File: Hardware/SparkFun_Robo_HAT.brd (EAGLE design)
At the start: 65.1 x 57 mm, 244 parts, among them J11 EXT MTR PWR, J18 ISP, J2 RASPBERRYPI-40-PIN-GPIO_SMD_S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, J20 USB C, J23 CORTEX_JTAG_DEBUG_PTH, J7 EXT SERVO PWR, J8 EXT 5V PWR, Q1 310mA/60V/1.6Ω, Q23 20V/0.2A/8MHz/1.2Ω/1Vth, Q24 20V/0.2A/8MHz/1.2Ω/1Vth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

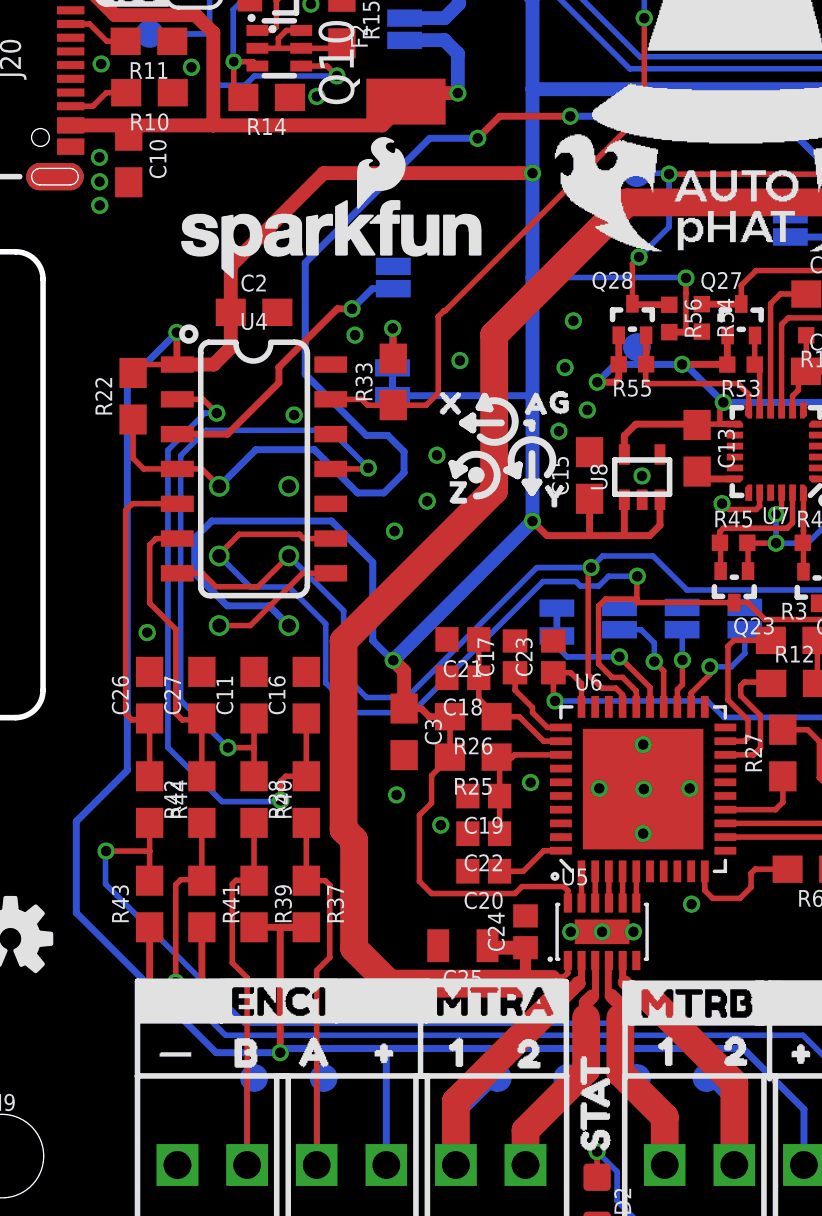
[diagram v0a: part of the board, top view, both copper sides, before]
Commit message: added test point to 3.3V rail
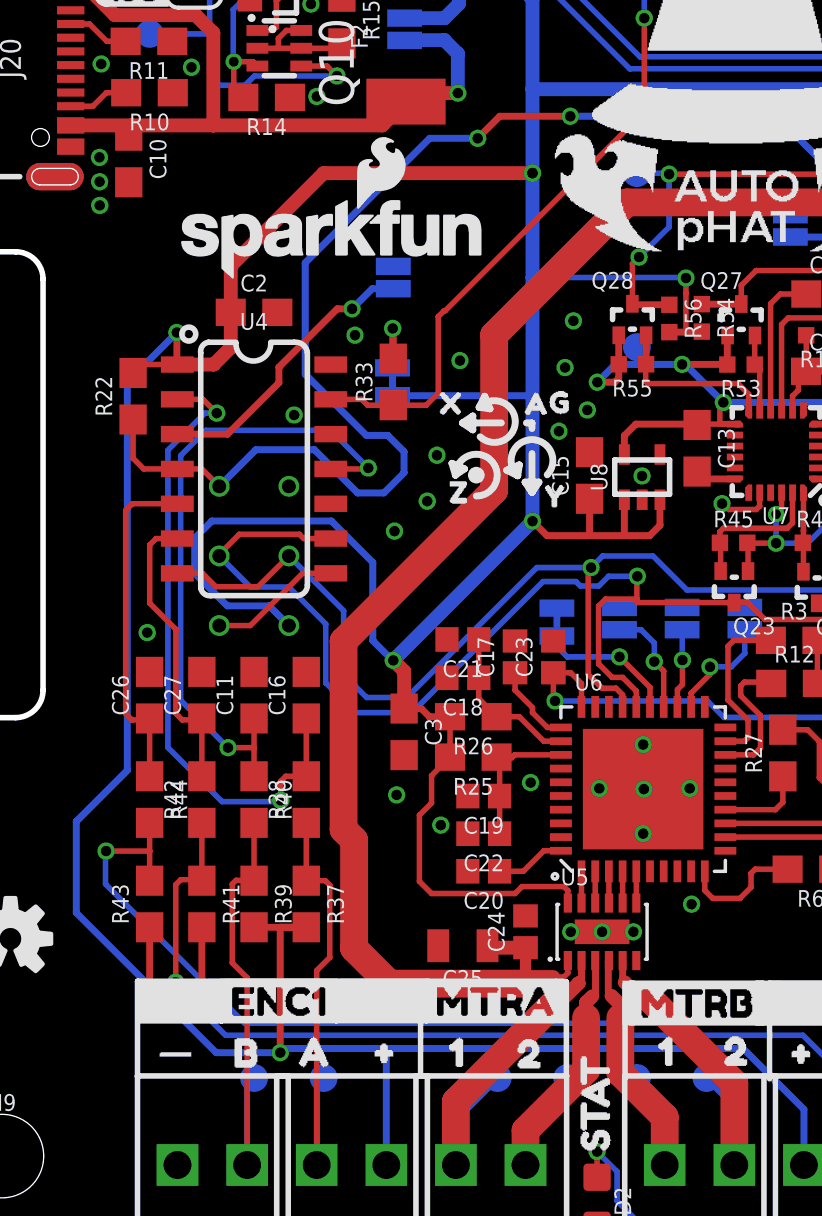
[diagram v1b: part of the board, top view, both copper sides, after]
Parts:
- added TP19: (no value), SparkFun-Connectors:TP_15TH
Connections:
- net 3.3V: now also TP19.P$1
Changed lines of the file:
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@@
 <grid distance="0.05" unitdist="inch" unit="inch" style="lines" multiple="1" display="yes" altdistance="0.001" altunitdist="inch" altunit="inch"/>
 <layers>
-<layer number="1" name="Top" color="4" fill="1" visible="yes" active="yes"/>
+<layer number="1" name="Top" color="4" fill="1" visible="no" active="yes"/>
 <layer number="15" name="Route15" color="4" fill="6" visible="no" active="no"/>
 <layer number="16" name="Bottom" color="1" fill="1" visible="yes" active="yes"/>
@@
 <layer number="18" name="Vias" color="2" fill="1" visible="yes" active="yes"/>
 <layer number="19" name="Unrouted" color="6" fill="1" visible="yes" active="yes"/>
-<layer number="20" name="Dimension" color="24" fill="1" visible="yes" active="yes"/>
-<layer number="21" name="tPlace" color="16" fill="1" visible="yes" active="yes"/>
+<layer number="20" name="Dimension" color="24" fill="1" visible="no" active="yes"/>
+<layer number="21" name="tPlace" color="16" fill="1" visible="no" active="yes"/>
 <layer number="22" name="bPlace" color="14" fill="1" visible="yes" active="yes"/>
-<layer number="23" name="tOrigins" color="15" fill="1" visible="yes" active="yes"/>
+<layer number="23" name="tOrigins" color="15" fill="1" visible="no" active="yes"/>
 <layer number="24" name="bOrigins" color="15" fill="1" visible="yes" active="yes"/>
 <layer number="25" name="tNames" color="7" fill="1" visible="no" active="yes"/>
@@
 <layer number="28" name="bValues" color="7" fill="1" visible="no" active="yes"/>
 <layer number="29" name="tStop" color="7" fill="3" visible="no" active="yes"/>
-<layer number="30" name="bStop" color="7" fill="6" visible="no" active="yes"/>
+<layer number="30" name="bStop" color="7" fill="6" visible="yes" active="yes"/>
 <layer number="31" name="tCream" color="7" fill="4" visible="no" active="yes"/>
 <layer number="32" name="bCream" color="7" fill="5" visible="no" active="yes"/>
@@
 <layer number="43" name="vRestrict" color="2" fill="10" visible="no" active="yes"/>
 <layer number="44" name="Drills" color="7" fill="1" visible="no" active="yes"/>
-<layer number="45" name="Holes" color="7" fill="1" visible="yes" active="yes"/>
+<layer number="45" name="Holes" color="7" fill="1" visible="no" active="yes"/>
 <layer number="46" name="Milling" color="3" fill="1" visible="no" active="yes"/>
 <layer number="47" name="Measures" color="7" fill="1" visible="no" active="yes"/>
 <layer number="48" name="Document" color="13" fill="7" visible="no" active="yes"/>
-<layer number="49" name="Reference" color="13" fill="1" visible="yes" active="yes"/>
+<layer number="49" name="Reference" color="13" fill="1" visible="no" active="yes"/>
 <layer number="50" name="dxf" color="7" fill="1" visible="no" active="yes"/>
-<layer number="51" name="tDocu" color="6" fill="1" visible="yes" active="yes"/>
+<layer number="51" name="tDocu" color="6" fill="1" visible="no" active="yes"/>
 <layer number="52" name="bDocu" color="7" fill="1" visible="no" active="yes"/>
 <layer number="91" name="Nets" color="2" fill="1" visible="no" active="no"/>
@@
 <element name="TP17" library="SparkFun-Connectors" package="PAD.03X.04" value="" x="15.24" y="6.35" smashed="yes" rot="MR0"/>
 <element name="TP18" library="SparkFun-Connectors" package="PAD.03X.04" value="" x="12.7" y="6.35" smashed="yes" rot="MR0"/>
+<element name="TP19" library="SparkFun-Connectors" package="TP_15TH" value="" x="22.86" y="39.37" smashed="yes" rot="MR0"/>
 </elements>
 <signals>
@@
 <wire x1="8.89" y1="9.0932" x2="8.89" y2="11.85" width="0.254" layer="1"/>
 <wire x1="30.543503125" y1="7.426959375" x2="32.766" y2="5.2044625" width="0.254" layer="16"/>
-<wire x1="16.678909375" y1="7.426959375" x2="16.5354" y2="7.426959375" width="0.254" layer="16"/>
-<wire x1="16.5354" y1="7.426959375" x2="13.807440625" y2="7.426959375" width="0.254" layer="16"/>
+<wire x1="17.526" y1="7.426959375" x2="13.807440625" y2="7.426959375" width="0.254" layer="16"/>
 <wire x1="13.807440625" y1="7.426959375" x2="13.655040625" y2="7.274559375" width="0.254" layer="16"/>
 <wire x1="13.655040625" y1="7.274559375" x2="11.318240625" y2="7.274559375" width="0.254" layer="16"/>
@@
 <wire x1="8.372" y1="49.7555" x2="8.372" y2="51.933" width="0.508" layer="1"/>
 <wire x1="8.372" y1="51.933" x2="8.382" y2="51.943" width="0.508" layer="1"/>
-<wire x1="16.678909375" y1="7.426959375" x2="17.526" y2="7.426959375" width="0.254" layer="16"/>
 <wire x1="17.526" y1="7.426959375" x2="30.543503125" y2="7.426959375" width="0.254" layer="16"/>
 <wire x1="17.526" y1="3.175" x2="17.526" y2="7.426959375" width="0.254" layer="16"/>
+<contactref element="TP19" pad="P$1"/>
 </signal>
 <signal name="5V">

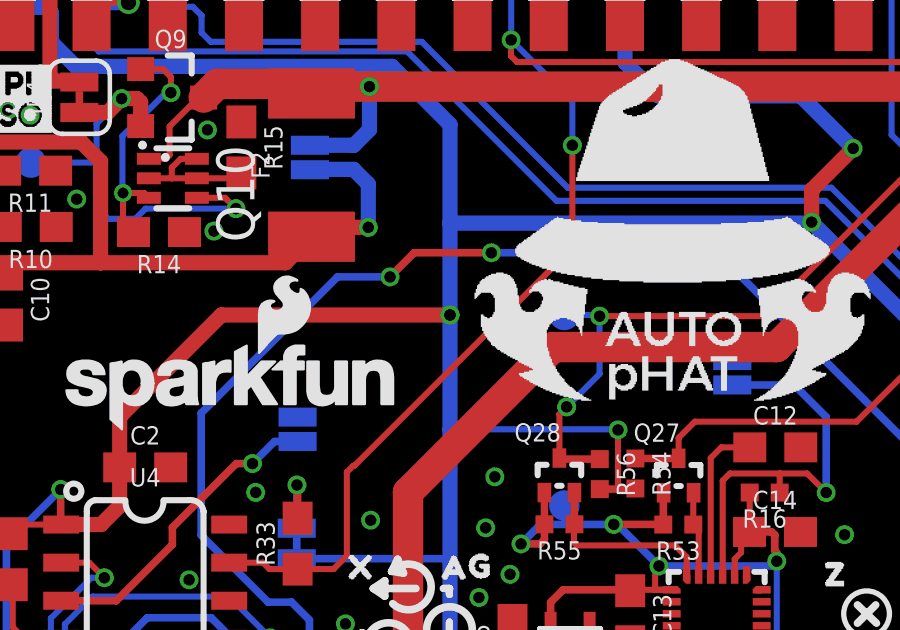
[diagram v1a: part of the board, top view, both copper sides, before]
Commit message: Cleaned up and fixed dimensions
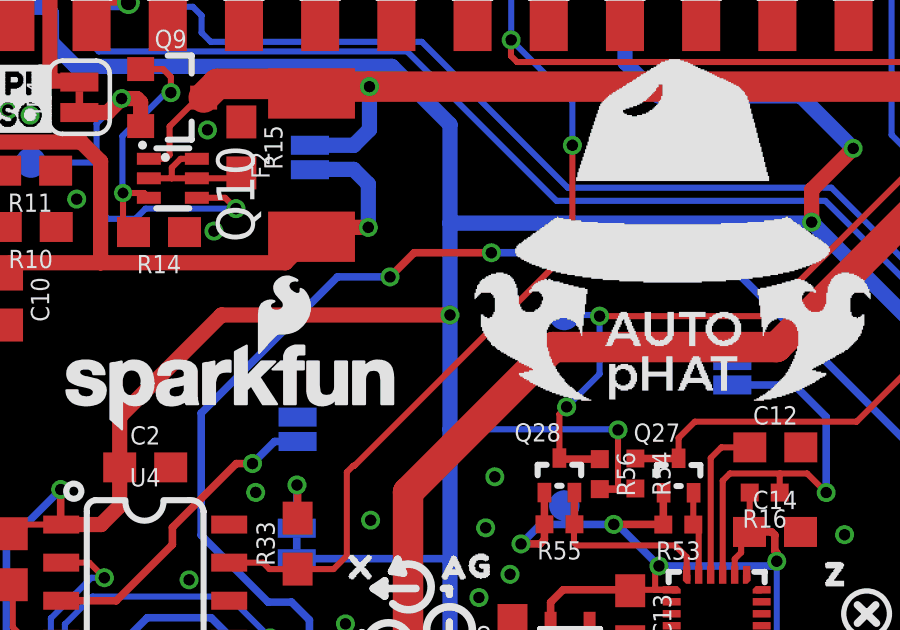
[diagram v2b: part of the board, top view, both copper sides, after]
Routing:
- net 3.3V: vias 15 -> 14

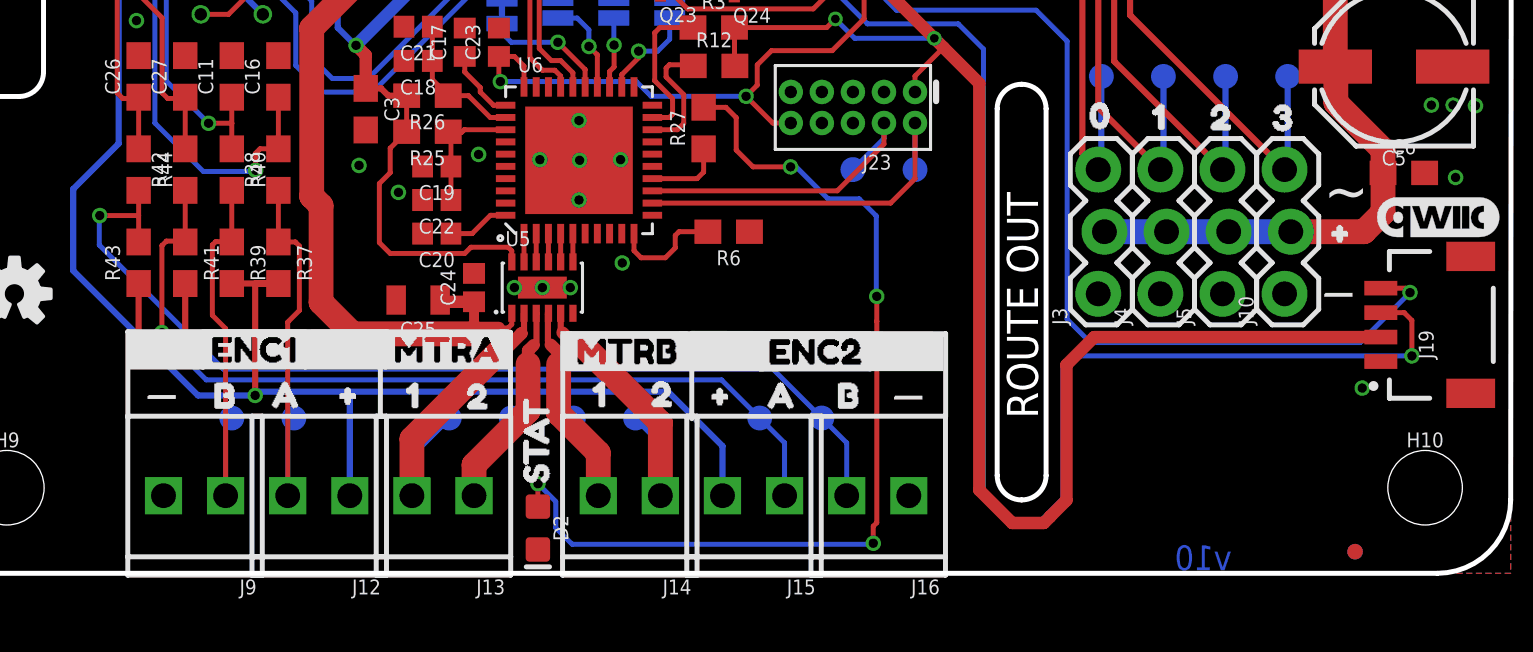
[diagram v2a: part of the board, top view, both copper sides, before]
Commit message: fixed vector font issue on servo "~"
-bumped version to v11
-also updated the "+" and "-" symbols on servo headers and encoder terminals (on both top silk and bottom silk) I drew everything with wires so they look clean and will hold position through the panelizer ulp tool
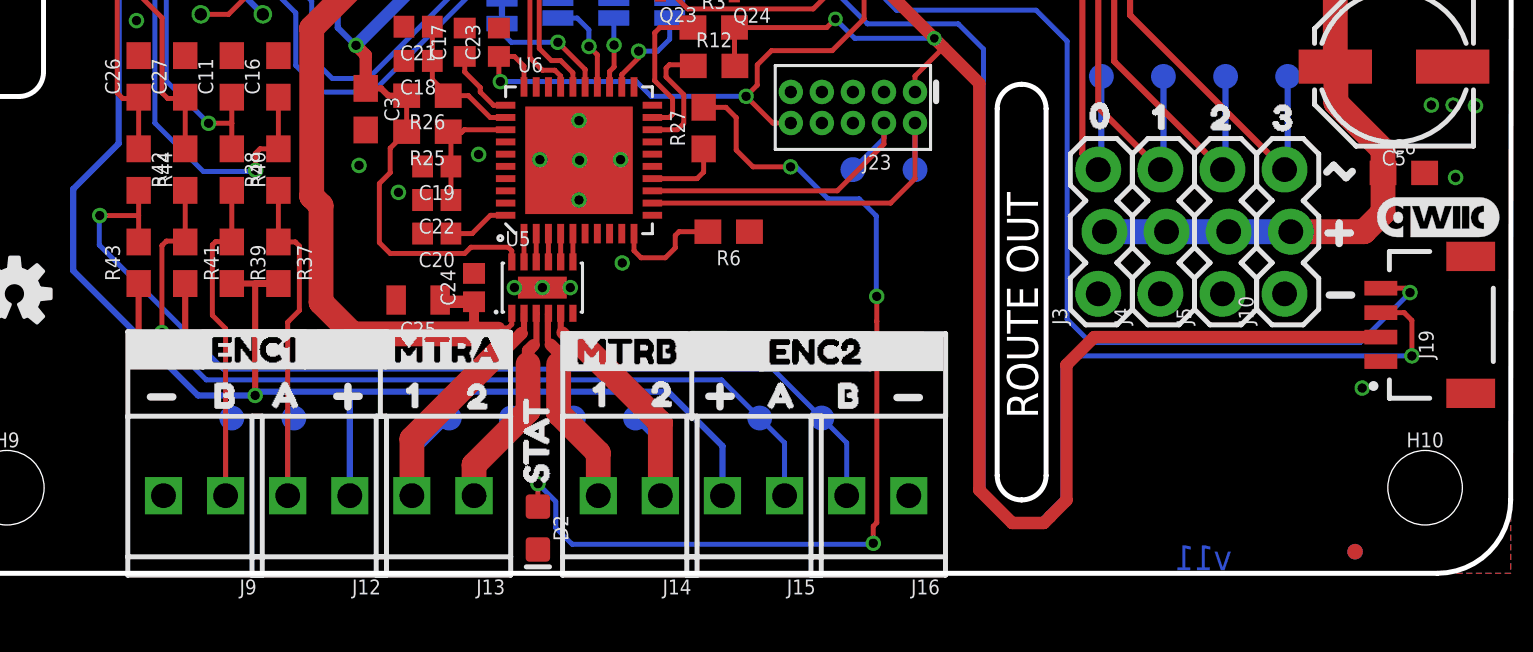
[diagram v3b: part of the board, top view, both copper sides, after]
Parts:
- removed U$18, U$19, U$41, U$47, U$63, U$64: (no value), buzzard_labels (2):#16
- removed U$28, U$30, U$38, U$46, U$71, U$72: (no value), buzzard_labels (2):_17
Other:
- board text added: "v11"
- board text removed: "v10"
- board text removed: "~"
